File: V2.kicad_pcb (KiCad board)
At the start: 2 copper layers, 76 parts, among them J20 Boot0, J21 Bed Temp, J22 Boot1, J26 USB_A, J27 LCD, J3 Bed Heater, J31 Bed level, J32 USB_B, J6 Head2, J7 Head1, M3 Motor Z2, M4 Motor Z1, M5 Motor Y, M6 Motor X, Q1 STN4NF20L, Q2 STN4NF20L, Q3 04N03LA, Q4 04N03LA, Q5 04N03LA, Q6 04N03LA, SW10 Button DOWN, SW11 Button UP, SW2 Boundary X, SW3 Boundary Y, SW4 Boundary Z1, SW5 Boundary Z2, SW6 Boundary E1, SW7 Boundary E2, SW8 Button BACK, SW9 Button OK, U1 LM2596S-5, U2 R-783.3-1.0, U3 STM32F105VCT6, U4 CP2104, Y1 hc49s

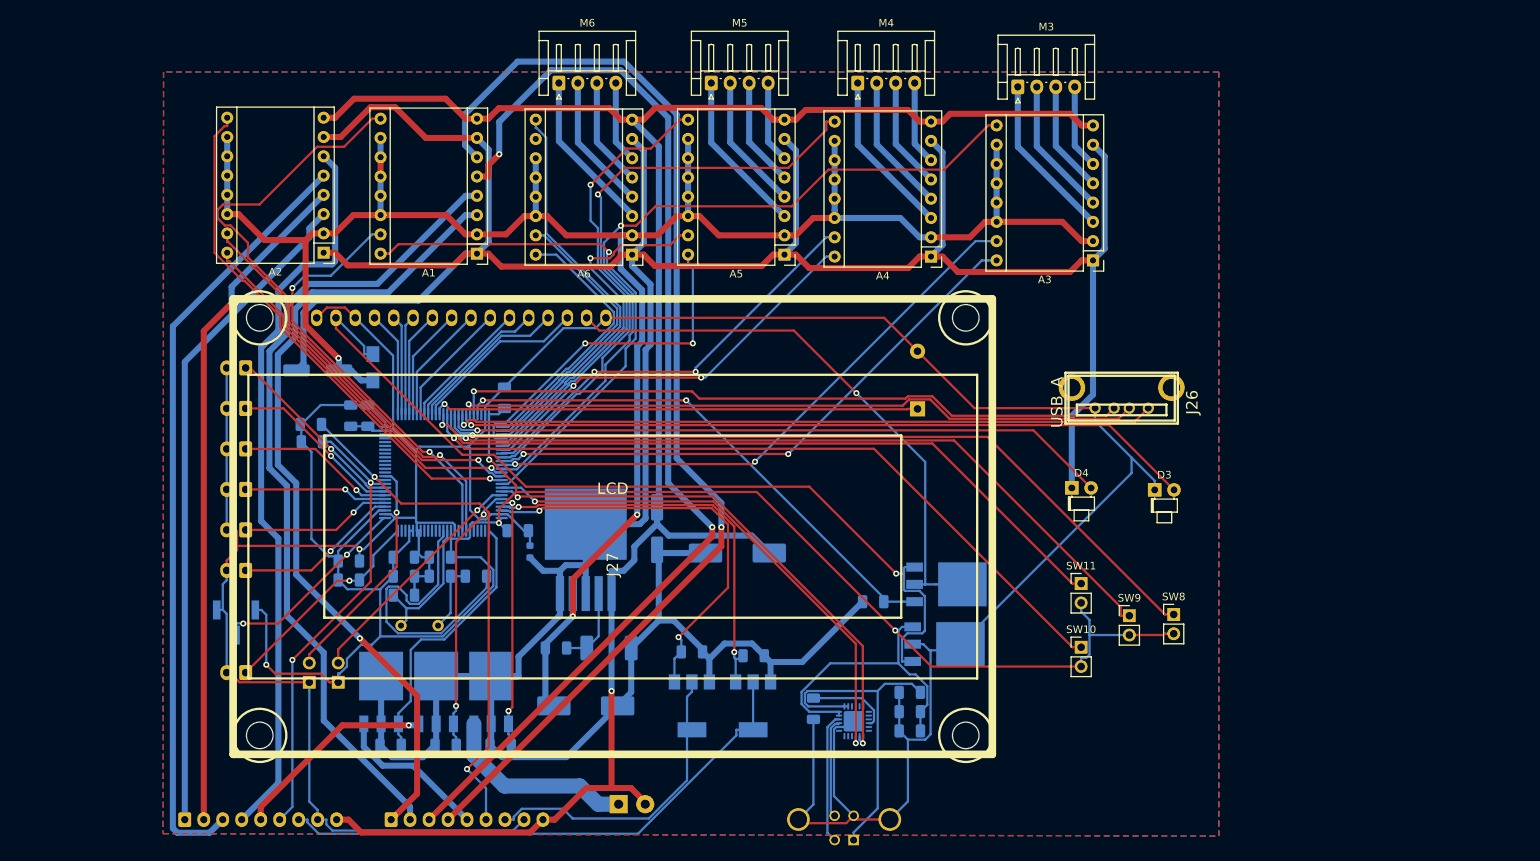
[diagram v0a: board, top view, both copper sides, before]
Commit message: Драйвера перенесены вбок, новая распиновка
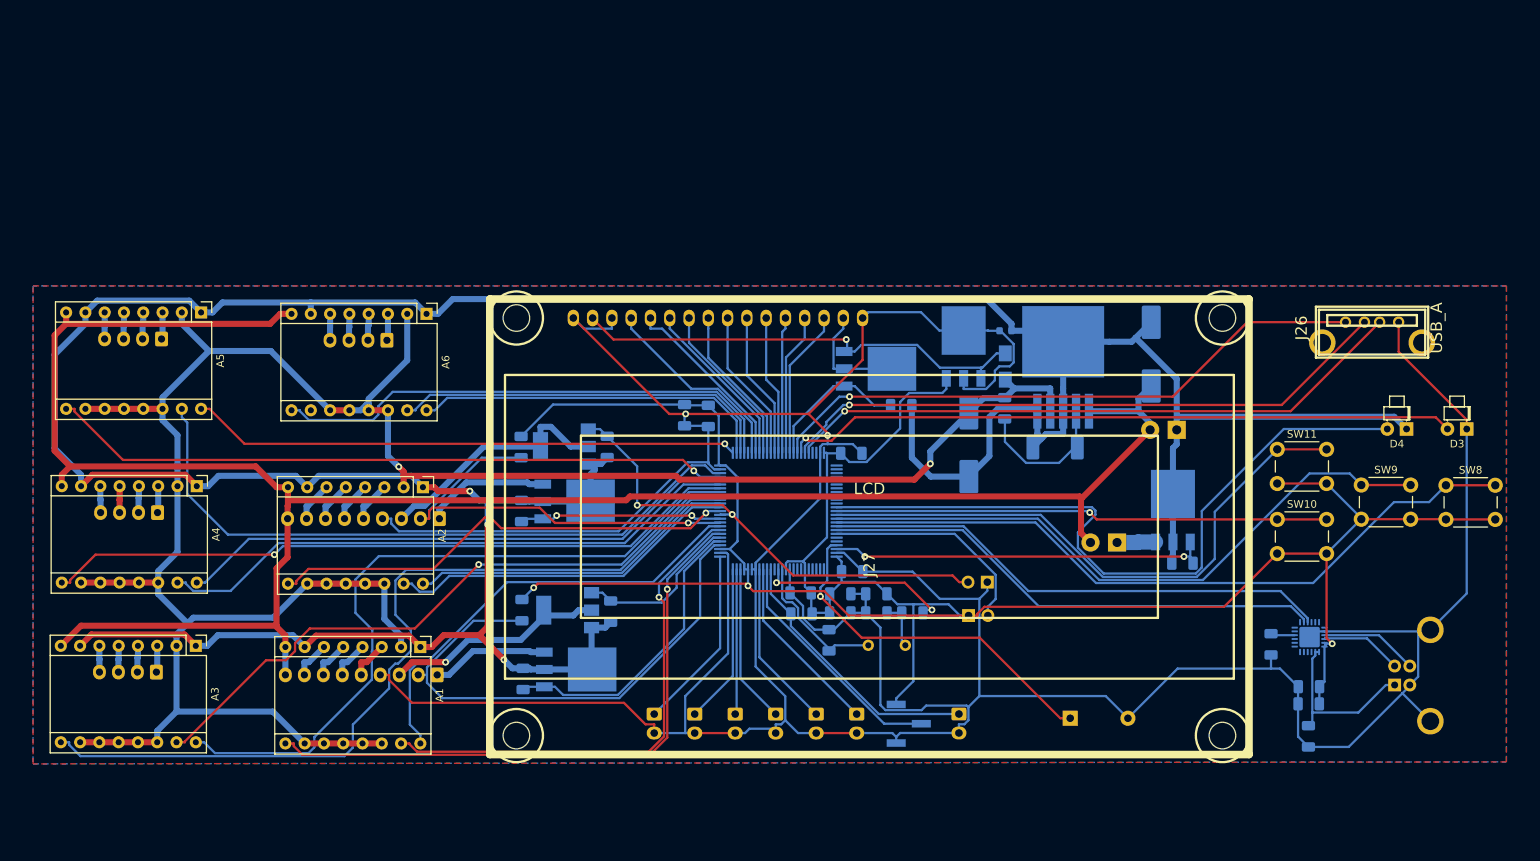
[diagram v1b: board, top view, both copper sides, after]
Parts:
- removed 33uH1: L?, Inductor_SMD:L_1206_3216Metric
- removed C7, C9: 33uF, Capacitor_SMD:CP_Elec_6.3x5.4
- added 47uH1: L?, Inductor_SMD:L_1206_3216Metric, B.Cu at (176.6, 95.9)
- added J1: Input voltage, TerminalBlock_4Ucon:TerminalBlock_4Ucon_1x02_P3.50mm_Horizontal, B.Cu at (199.2, 98.8)
- J32: footprint Connector_USB:USB_B_Amphenol_MUSB-D511_Vertical_Rugged -> Connector_USB:USB_B_OST_USB-B1HSxx_Horizontal
- M3, M4, M5, M6: footprint Connector_JST:JST_EH_S04B-EH_1x04_P2.50mm_Horizontal -> Connector_JST:JST_EH_B04B-EH-A_1x04_P2.50mm_Vertical; moved to B.Cu
- SW10, SW11, SW8, SW9: footprint Connector_PinHeader_2.54mm:PinHeader_1x02_P2.54mm_Vertical -> Button_Switch_THT:SW_PUSH_6mm
- moved M3 137.2 mm to (64.8, 130.7), turned to 180 degrees
- moved A3 128.6 mm to (70.0, 127.2), turned to 270 degrees
- moved M4 108.2 mm to (65.0, 109.7), turned to 180 degrees
- moved A4 101.3 mm to (70.2, 106.2), turned to 270 degrees
- moved J21 94.1 mm to (170.6, 136.2), turned to 270 degrees
- moved Q3 92.9 mm to (198.7, 109.3)
- moved R3 92.9 mm to (200.0, 116.3)
- moved J22 90.3 mm to (174.3, 118.8), turned to 90 degrees
- moved J31 89.6 mm to (163.9, 137.5), turned to 0 degrees
- moved J20 83.5 mm to (171.8, 123.2), turned to 270 degrees
- moved D2 83.3 mm to (176.7, 90.4)
- moved SW2 82.7 mm to (157.1, 136.2), turned to 270 degrees
- moved M5 79.9 mm to (65.5, 86.8), turned to 180 degrees
- moved SW3 79.0 mm to (151.8, 136.2), turned to 270 degrees
- moved A5 77.2 mm to (70.7, 83.3), turned to 270 degrees
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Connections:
- J6 pad 1: Net-(A1-Pad3) -> Net-(J6-Pad1)
- J6 pad 2: Net-(A1-Pad4) -> Net-(J6-Pad2)
- J6 pad 3: Net-(A1-Pad5) -> Net-(J6-Pad3)
- J6 pad 4: Net-(A1-Pad6) -> GNDD
- J6 pad 5: Net-(J6-Pad5) -> Net-(A1-Pad3)
- J6 pad 6: Net-(J6-Pad6) -> Net-(A1-Pad4)
- J6 pad 7: Net-(J6-Pad7) -> Net-(A1-Pad5)
- J6 pad 8: GNDD -> Net-(A1-Pad6)
- J7 pad 1: Net-(A2-Pad3) -> Net-(J7-Pad1)
- J7 pad 2: Net-(A2-Pad4) -> Net-(J7-Pad2)
- J7 pad 3: Net-(A2-Pad5) -> Net-(J7-Pad3)
- J7 pad 4: Net-(A2-Pad6) -> GNDD
- J7 pad 5: Net-(J7-Pad5) -> Net-(A2-Pad3)
- J7 pad 6: Net-(J7-Pad6) -> Net-(A2-Pad4)
- J7 pad 7: Net-(J7-Pad7) -> Net-(A2-Pad5)
- J7 pad 8: GNDD -> Net-(A2-Pad6)
- Q1 pad 2: Net-(J6-Pad7) -> Net-(J6-Pad3)
- Q2 pad 1: Net-(Q2-Pad1) -> Net-(J22-Pad2)
- Q2 pad 2: Net-(J7-Pad7) -> Net-(J7-Pad3)
- Q4 pad 3: Net-(J7-Pad5) -> Net-(J7-Pad1)
- Q5 pad 3: Net-(J6-Pad5) -> Net-(J6-Pad1)
- R2 pad 2: Net-(Q2-Pad1) -> Net-(J22-Pad2)
- R8 pad 1: Net-(J7-Pad6) -> Net-(J7-Pad2)
- R9 pad 1: Net-(J6-Pad6) -> Net-(J6-Pad2)
- U3 pad 1: Net-(Q5-Pad1) -> Net-(U3-Pad1)
- U3 pad 15: Net-(U3-Pad15) -> Net-(J21-Pad1)
- U3 pad 16: Net-(U3-Pad16) -> Net-(J31-Pad2)
- U3 pad 17: Net-(U3-Pad17) -> Net-(SW2-Pad1)
- U3 pad 18: Net-(U3-Pad18) -> Net-(SW3-Pad1)
- U3 pad 23: Net-(U3-Pad23) -> Net-(SW4-Pad1)
- U3 pad 24: Net-(U3-Pad24) -> Net-(SW5-Pad1)
- U3 pad 25: Net-(J21-Pad1) -> Net-(SW6-Pad1)
- U3 pad 26: Net-(J31-Pad2) -> Net-(SW7-Pad1)
- U3 pad 29: Net-(SW2-Pad1) -> Net-(J6-Pad2)
- U3 pad 30: Net-(SW3-Pad1) -> Net-(Q5-Pad1)
- U3 pad 31: Net-(SW4-Pad1) -> Net-(Q1-Pad1)
- U3 pad 32: Net-(SW5-Pad1) -> Net-(A1-Pad9)
- U3 pad 33: Net-(SW6-Pad1) -> Net-(A1-Pad15)
- U3 pad 34: Net-(SW7-Pad1) -> Net-(A1-Pad16)
- U3 pad 35: Net-(J7-Pad6) -> Net-(J7-Pad2)
- U3 pad 36: Net-(J6-Pad6) -> Net-(Q4-Pad1)
- U3 pad 38: Net-(U3-Pad38) -> Net-(A2-Pad9)
- U3 pad 39: Net-(U3-Pad39) -> Net-(A2-Pad15)
- U3 pad 40: Net-(U3-Pad40) -> Net-(A2-Pad16)
- U3 pad 41: Net-(U3-Pad41) -> Net-(A3-Pad9)
- U3 pad 42: Net-(U3-Pad42) -> Net-(A3-Pad15)
- U3 pad 43: Net-(U3-Pad43) -> Net-(A3-Pad16)
- U3 pad 44: Net-(U3-Pad44) -> Net-(A4-Pad9)
- U3 pad 45: Net-(U3-Pad45) -> Net-(A4-Pad15)
- U3 pad 46: Net-(U3-Pad46) -> Net-(A4-Pad16)
- U3 pad 47: Net-(U3-Pad47) -> Net-(A5-Pad9)
- U3 pad 48: Net-(U3-Pad48) -> Net-(A5-Pad15)
- U3 pad 51: Net-(J27-Pad4) -> Net-(A5-Pad16)
- U3 pad 52: Net-(J27-Pad5) -> Net-(A6-Pad16)
- U3 pad 53: Net-(J27-Pad6) -> Net-(A6-Pad15)
- U3 pad 54: Net-(J27-Pad7) -> Net-(A6-Pad9)
- U3 pad 55: Net-(J27-Pad8) -> Net-(U3-Pad55)
- U3 pad 56: Net-(J27-Pad9) -> Net-(J27-Pad4)
- U3 pad 57: Net-(J27-Pad10) -> Net-(J27-Pad5)
- U3 pad 58: Net-(J27-Pad11) -> Net-(J27-Pad6)
- U3 pad 59: Net-(J27-Pad12) -> Net-(J27-Pad7)
- U3 pad 60: Net-(J27-Pad13) -> Net-(J27-Pad8)
- U3 pad 61: Net-(J27-Pad14) -> Net-(J27-Pad9)
- U3 pad 62: Net-(LS1-Pad1) -> Net-(J27-Pad10)
- U3 pad 63: Net-(SW11-Pad1) -> Net-(J27-Pad11)
- U3 pad 64: Net-(SW10-Pad1) -> Net-(J27-Pad12)
- U3 pad 65: Net-(SW9-Pad1) -> Net-(J27-Pad13)
- U3 pad 66: Net-(SW8-Pad1) -> Net-(J27-Pad14)
- U3 pad 67: Net-(D4-Pad2) -> Net-(Q6-Pad1)
- U3 pad 7: Net-(A1-Pad9) -> Net-(U3-Pad7)
- U3 pad 72: Net-(Q6-Pad1) -> Net-(U3-Pad72)
- U3 pad 76: Net-(A6-Pad16) -> Net-(U3-Pad76)
- U3 pad 77: Net-(A6-Pad15) -> Net-(U3-Pad77)
- U3 pad 78: Net-(A6-Pad9) -> Net-(U3-Pad78)
- U3 pad 79: Net-(A5-Pad16) -> Net-(U3-Pad79)
- U3 pad 8: Net-(A1-Pad15) -> Net-(U3-Pad8)
- U3 pad 80: Net-(A5-Pad15) -> Net-(U3-Pad80)
- U3 pad 81: Net-(A5-Pad9) -> Net-(U3-Pad81)
- U3 pad 82: Net-(A4-Pad16) -> Net-(U3-Pad82)
- U3 pad 83: Net-(A4-Pad15) -> Net-(U3-Pad83)
- U3 pad 84: Net-(A4-Pad9) -> Net-(U3-Pad84)
- U3 pad 85: Net-(A3-Pad16) -> Net-(U3-Pad85)
- U3 pad 86: Net-(A3-Pad15) -> Net-(U3-Pad86)
- U3 pad 87: Net-(A3-Pad9) -> Net-(D4-Pad2)
- U3 pad 88: Net-(A2-Pad16) -> Net-(SW10-Pad1)
- U3 pad 89: Net-(A2-Pad15) -> Net-(SW11-Pad1)
- U3 pad 90: Net-(A2-Pad9) -> Net-(SW9-Pad1)
- U3 pad 91: Net-(A1-Pad16) -> Net-(SW8-Pad1)
- U3 pad 95: Net-(Q4-Pad1) -> Net-(U3-Pad95)
- U3 pad 96: Net-(Q3-Pad1) -> Net-(U3-Pad96)
- U3 pad 97: Net-(Q2-Pad1) -> Net-(LS1-Pad1)
- U3 pad 98: Net-(Q1-Pad1) -> Net-(Q3-Pad1)
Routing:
- net Net-(A1-Pad6): track 150.2 -> 5.08 mm, vias 1 -> 0
- net Net-(A1-Pad5): track 147.3 -> 5.12 mm, vias 2 -> 0
- net GNDD: track 446.3 -> 555.5 mm, vias 1 -> 2
- net Net-(A1-Pad4): track 107.4 -> 5.16 mm
- net Net-(A1-Pad3): track 106.3 -> 5.20 mm, vias 1 -> 0
- net Net-(A2-Pad5): track 101.7 -> 5.37 mm
- net Net-(A2-Pad6): track 97.1 -> 5.33 mm
- net Net-(A2-Pad4): track 88.8 -> 5.41 mm, vias 1 -> 0
- net Net-(A2-Pad3): track 87.3 -> 5.45 mm
- net Net-(J7-Pad7): track 73.5 -> 0.00 mm
- net Net-(J6-Pad6): track 71.1 -> 0.00 mm, vias 2 -> 0
- net Net-(J6-Pad2): track 0.00 -> 70.5 mm
- net Net-(J7-Pad6): track 60.0 -> 0.00 mm, vias 2 -> 0
- net Net-(J27-Pad15): track 74.9 -> 14.9 mm, vias 1 -> 0
- net Net-(J7-Pad2): track 0.00 -> 58.7 mm, vias 0 -> 1
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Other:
- net class Bed: via_dia 0.8 -> 0.9; via_drill 0.4 -> 0.8
- net class Default: via_dia 0.8 -> 0.9; via_drill 0.4 -> 0.8
- net class High Current: via_dia 0.8 -> 0.9; via_drill 0.4 -> 0.8

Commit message: Vias clearence and vias diameter are increased
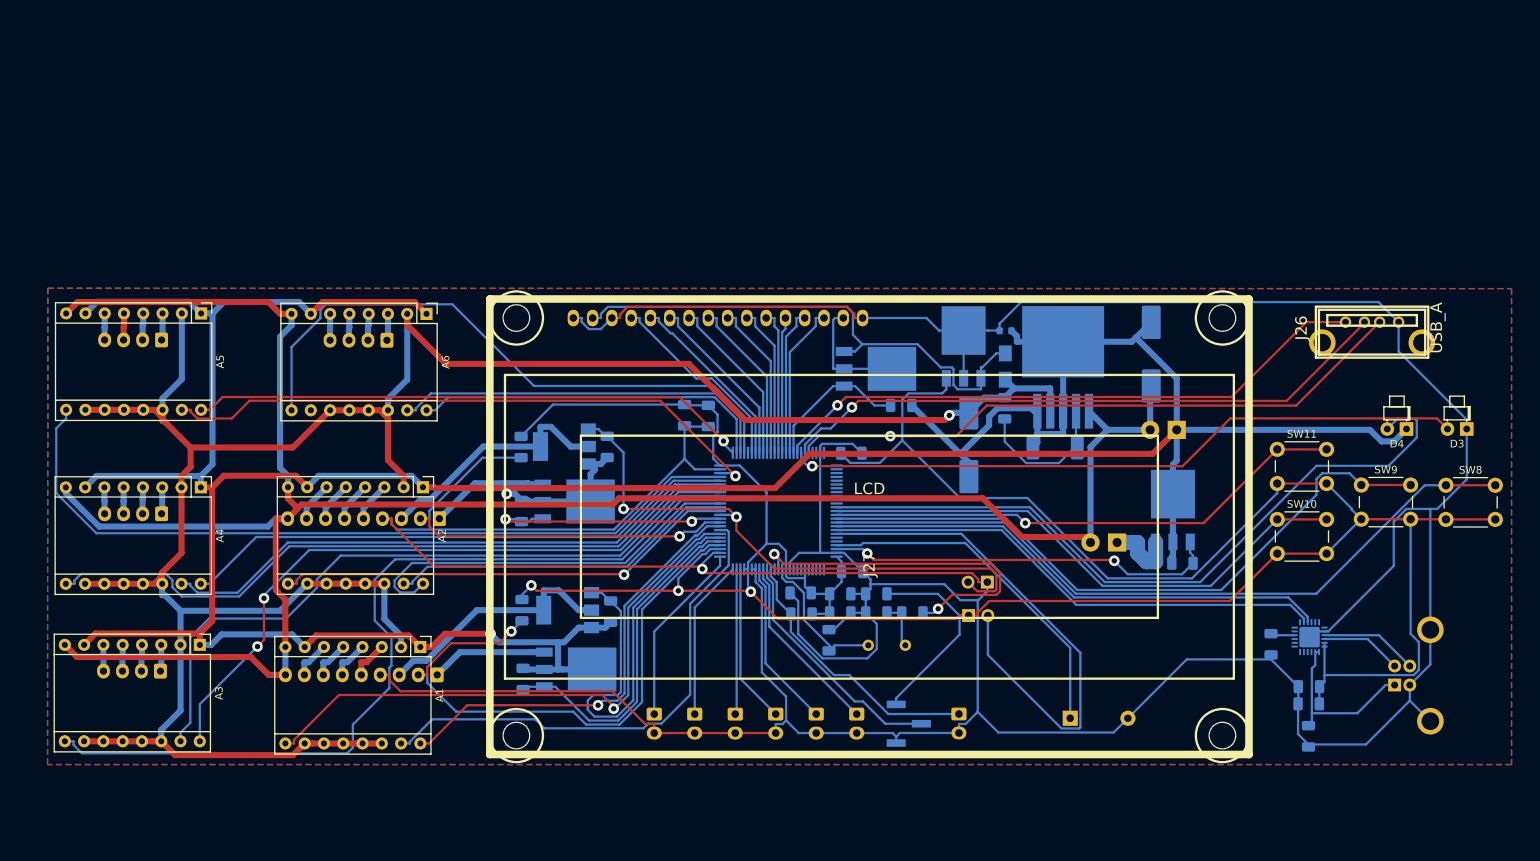
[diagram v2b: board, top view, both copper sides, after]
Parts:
- moved A4 0.55 mm to (70.7, 106.3)
- moved M4 0.55 mm to (65.5, 109.8)
- moved A3 0.55 mm to (70.6, 127.1)
- moved M3 0.55 mm to (65.4, 130.6)
- moved M5 0.13 mm to (65.5, 86.9)
- moved A5 0.13 mm to (70.7, 83.4)
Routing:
- net GNDD: track 555.5 -> 640.4 mm, vias 2 -> 1
- net +3V3: track 319.5 -> 398.5 mm
- net Net-(J20-Pad2): track 29.0 -> 69.9 mm
- net Net-(Q1-Pad1): track 22.0 -> 56.3 mm
- net Net-(R7-Pad1): track 25.2 -> 46.7 mm
- net Net-(A5-Pad9): track 90.1 -> 104.2 mm, vias 1 -> 0
- net Net-(A6-Pad9): track 68.3 -> 81.9 mm
- net Net-(J22-Pad2): track 63.0 -> 75.7 mm
- net GND: track 470.0 -> 482.4 mm, vias 3 -> 2
- net Net-(SW11-Pad1): track 78.5 -> 69.0 mm, vias 0 -> 1
- net Net-(A2-Pad16): track 43.5 -> 52.5 mm
- net +5VD: track 61.3 -> 69.2 mm, vias 1 -> 0
- net Net-(A5-Pad15): track 88.1 -> 80.8 mm, vias 0 -> 1
- net Net-(SW10-Pad1): track 65.0 -> 72.2 mm, vias 1 -> 0
- net Net-(Q4-Pad1): track 26.7 -> 33.7 mm
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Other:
- net class Bed: via_dia 0.9 -> 1.4
- net class Default: clearance 0.1 -> 0.19; via_dia 0.9 -> 1.4
- net class High Current: via_dia 0.9 -> 1.4
- rule trace_clearance: 0.1 -> 0.19

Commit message: Новая версия
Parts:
- removed C11, C12, C13, C14: 100nF, Capacitor_SMD:C_1206_3216Metric
- removed J31: Bed level, Connector_PinHeader_2.54mm:PinHeader_1x03_P2.54mm_Vertical_SMD_Pin1Left
- added SW1: Bed Level nozle, Connector_JST:JST_EH_B02B-EH-A_1x02_P2.50mm_Vertical, B.Cu at (177.7, 136.3)
- added SW12: Bed Level, Connector_JST:JST_EH_B02B-EH-A_1x02_P2.50mm_Vertical, B.Cu at (164.2, 136.1)
- moved C10 30.1 mm to (136.5, 101.1), turned to 90 degrees
- moved C8 22.9 mm to (135.5, 119.8)
- moved R7 5.33 mm to (159.8, 120.3), turned to 0 degrees
- moved LS1 3.10 mm to (188.3, 136.2)
- moved R8 2.23 mm to (112.6, 98.8)
- moved Q4 2.23 mm to (119.7, 106.0)
- moved R4 2.23 mm to (112.7, 107.2)
- moved Q2 2.23 mm to (118.3, 98.8)
- moved R2 2.23 mm to (124.0, 98.8)
- moved J21 0.29 mm to (170.8, 136.1)
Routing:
- net Net-(Q3-Pad1): track 51.9 -> 144.4 mm, vias 2 -> 0
- net +3V3: track 398.5 -> 341.1 mm
- net GND: track 482.4 -> 538.2 mm, vias 2 -> 0
- net Net-(J20-Pad2): track 69.9 -> 24.9 mm
- net GNDD: track 640.4 -> 596.9 mm, vias 1 -> 2
- net Net-(SW1-Pad1): track 0.00 -> 38.6 mm
- net Net-(A4-Pad9): track 94.6 -> 129.4 mm
- net Net-(A4-Pad15): track 77.5 -> 104.5 mm
- net Net-(Q1-Pad1): track 56.3 -> 30.5 mm, vias 0 -> 2
- net Net-(J6-Pad2): track 77.2 -> 51.8 mm, vias 1 -> 2
- net Net-(D4-Pad2): track 95.2 -> 76.9 mm
- net Net-(R7-Pad1): track 46.7 -> 29.7 mm, vias 2 -> 0
- net Net-(A6-Pad9): track 81.9 -> 68.2 mm
- net +24V: track 283.7 -> 270.2 mm
- net Net-(A4-Pad16): track 74.0 -> 84.6 mm, vias 0 -> 1
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
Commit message: переразвёл заново
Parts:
- 47uH1: footprint Inductor_SMD:L_1206_3216Metric -> Inductor_THT:L_Radial_D12.0mm_P6.00mm_MuRATA_1900R
- C1: footprint Capacitor_SMD:CP_Elec_10x10.5 -> Capacitor_THT:CP_Radial_D10.0mm_P5.00mm
- C2: footprint Capacitor_SMD:CP_Elec_10x10.5 -> Capacitor_THT:CP_Radial_D10.0mm_P7.50mm
- D1: footprint Diode_SMD:D_2512_6332Metric_Castellated -> Diode_SMD:SS14
- D2: footprint w_smd_diode:do214ac -> w_smd_diode:do214ab
- J1, J3: footprint TerminalBlock_4Ucon:TerminalBlock_4Ucon_1x02_P3.50mm_Horizontal -> TerminalBlock_RND:TerminalBlock_RND_205-00045_1x02_P5.00mm_Horizontal
- Q1, Q2: footprint Package_TO_SOT_SMD:SOT-223-3_TabPin2 -> Package_TO_SOT_SMD:TO-252-2
- Q3, Q4, Q5, Q6: footprint Package_TO_SOT_SMD:TO-252-3_TabPin2 -> Package_TO_SOT_SMD:TO-252-2
- U2: footprint Package_TO_SOT_SMD:TO-252-3_TabPin2 -> Package_TO_SOT_SMD:SOT-223-3_TabPin2
- moved J22 55.6 mm to (125.1, 93.0), turned to 180 degrees
- moved R8 23.1 mm to (123.2, 119.4), turned to 180 degrees
- moved C10 20.4 mm to (156.8, 98.8), turned to 270 degrees
- moved C8 13.5 mm to (127.3, 130.4)
- moved 47uH1 13.0 mm to (180.4, 108.4), turned to 180 degrees
- moved R9 12.6 mm to (120.2, 132.8), turned to 180 degrees
- moved Q5 11.4 mm to (108.7, 131.0)
- moved R5 11.4 mm to (101.7, 132.3)
- moved Q1 11.4 mm to (107.6, 123.2)
- moved R6 9.52 mm to (178.6, 95.0), turned to 270 degrees
- moved R1 9.50 mm to (115.3, 124.0)
- moved Q6 9.39 mm to (167.5, 85.6), turned to 90 degrees
- moved C2 8.22 mm to (166.0, 106.5), turned to 90 degrees
- moved Q2 8.07 mm to (110.3, 98.2)
- moved Q4 8.07 mm to (111.6, 105.5)
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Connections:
- U2 pad 1: +5VD -> GNDD
- U2 pad 2: GNDD -> +3V3
- U2 pad 3: +3V3 -> +5VD
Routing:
- net GND: track 538.2 -> 415.7 mm, vias 0 -> 6
- net Net-(Q3-Pad1): track 144.4 -> 72.6 mm
- net +5V: track 311.5 -> 352.6 mm, vias 1 -> 3
- net +3V3: track 341.1 -> 376.3 mm
- net Net-(J22-Pad2): track 75.6 -> 43.4 mm, vias 2 -> 1
- net Net-(A4-Pad9): track 129.4 -> 98.0 mm
- net Net-(J27-Pad15): track 15.0 -> 46.4 mm
- net GNDD: track 596.9 -> 568.3 mm
- net +24V: track 270.2 -> 298.4 mm, vias 0 -> 3
- net Net-(A4-Pad15): track 104.5 -> 80.8 mm
- net Net-(SW11-Pad1): track 68.2 -> 82.8 mm
- net Net-(D4-Pad2): track 76.9 -> 90.4 mm
- net +5VD: track 72.9 -> 61.8 mm
- net Net-(J6-Pad2): track 51.8 -> 61.8 mm, vias 2 -> 1
- net Net-(Q6-Pad1): track 19.6 -> 28.3 mm
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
